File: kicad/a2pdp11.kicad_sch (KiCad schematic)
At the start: 44 parts, among them J1 DCJ11A, J2 DCJ11B, J3 TN9A, J4 TN9A, J5 A2BUSA, J6 A2BUSB, J7 3V3, J8 5V, J9 Jumper, SW1 HALT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

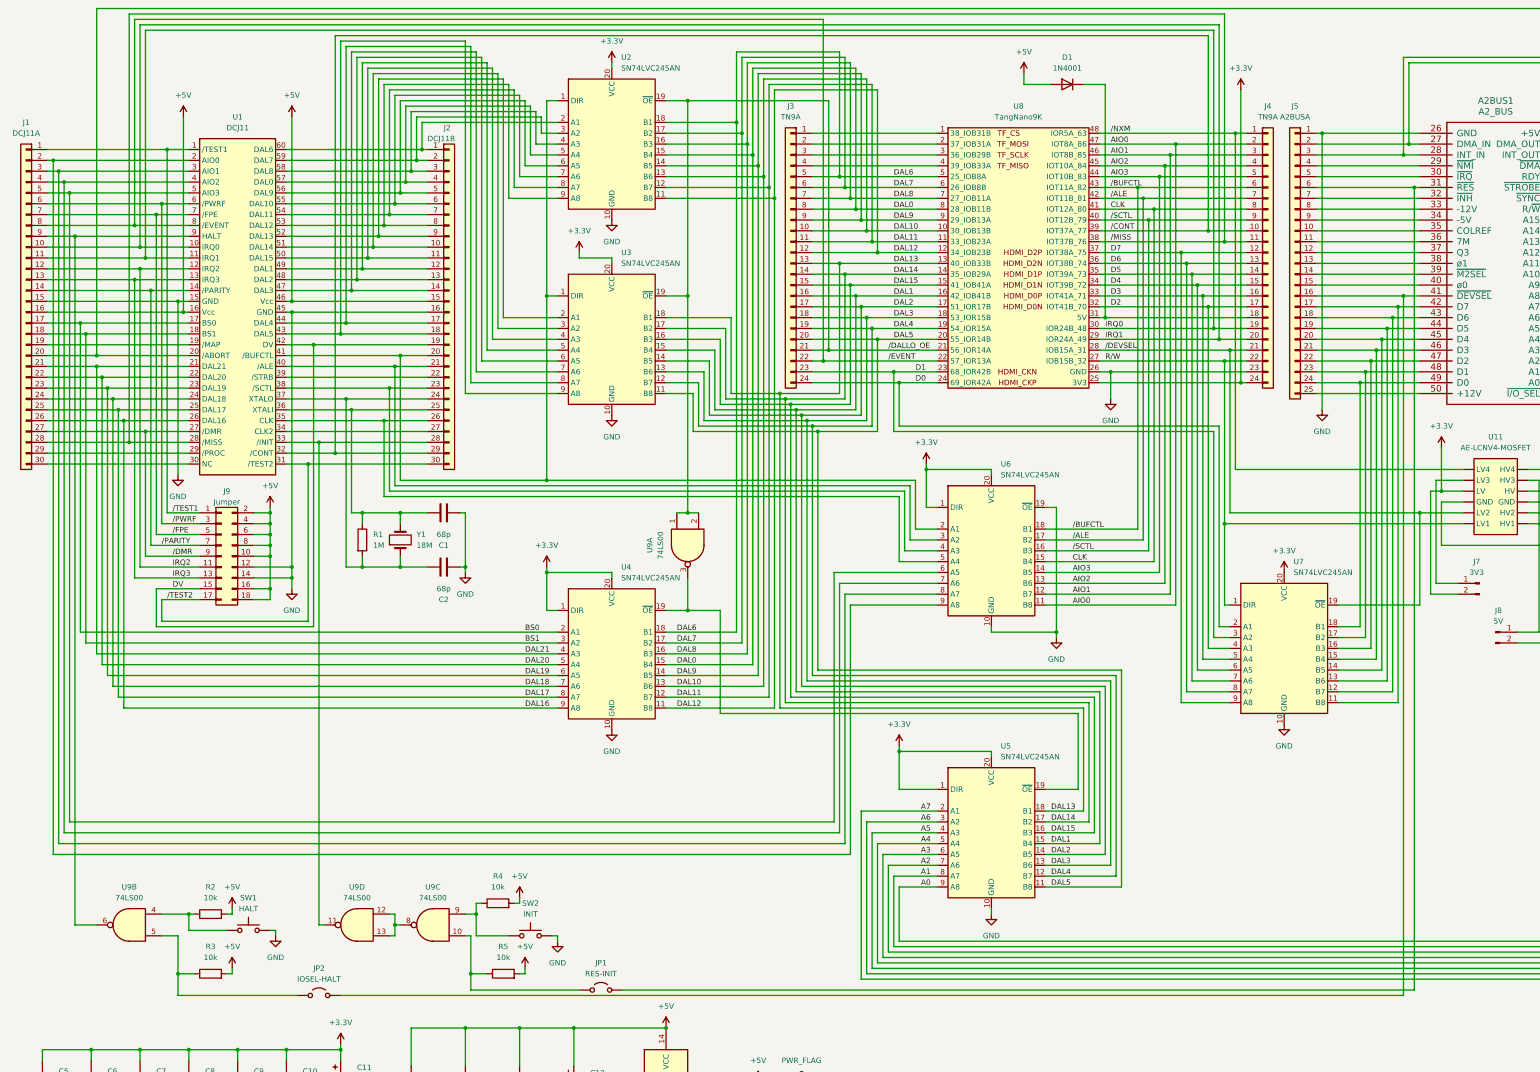
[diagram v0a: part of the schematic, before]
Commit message: Change I/O signal to IOSEL
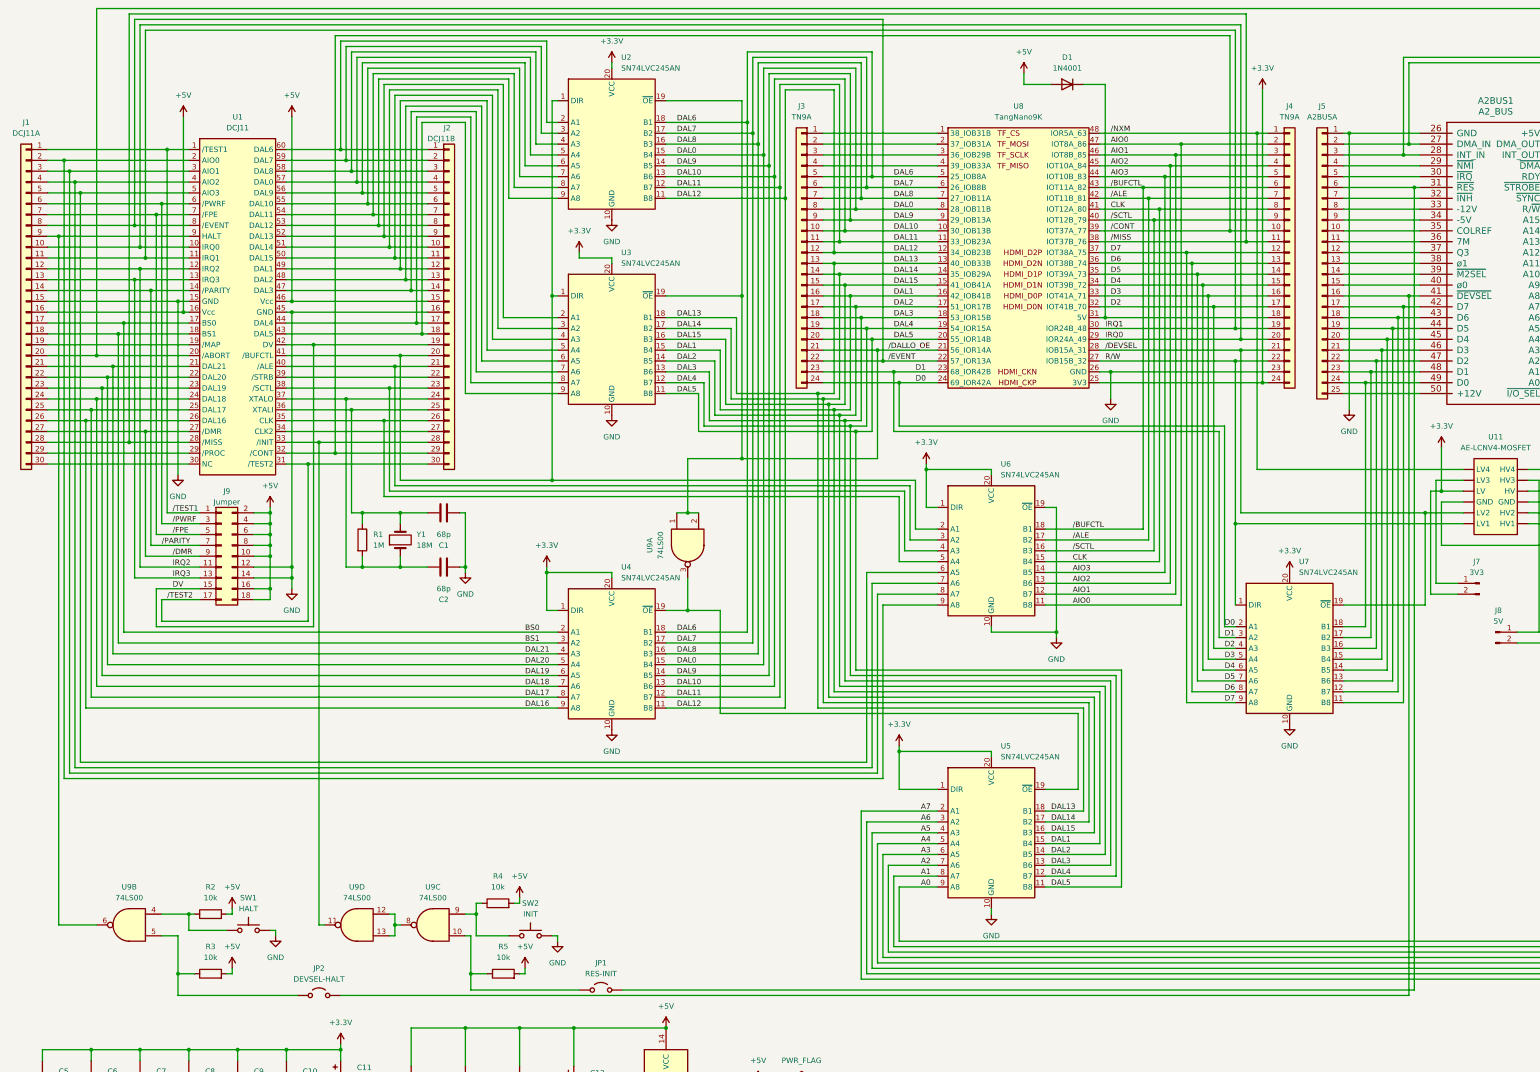
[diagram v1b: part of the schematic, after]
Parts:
- JP2: value IOSEL-HALT -> DEVSEL-HALT
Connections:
- net IRQ0: now also J1.10 (Pin_10), J4.20 (Pin_20), U1.10 (IRQ0), U8.29 (IOR24A_49); no longer J1.11 (Pin_11), J4.19 (Pin_19), U1.11 (IRQ1), U8.30 (IOR24B_48)
- net IRQ1: now also J1.11 (Pin_11), J4.19 (Pin_19), U1.11 (IRQ1), U8.30 (IOR24B_48); no longer J1.10 (Pin_10), J4.20 (Pin_20), U1.10 (IRQ0), U8.29 (IOR24A_49)
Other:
- title: J11 Test 16 -> J11 Test 17
- moved on the sheet: J3, J4, J5, U7
